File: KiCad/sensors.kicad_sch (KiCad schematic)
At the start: 26 parts, among them Q1 AO3401A, U6 LTR-303ALS-01, U8 GXHTC3

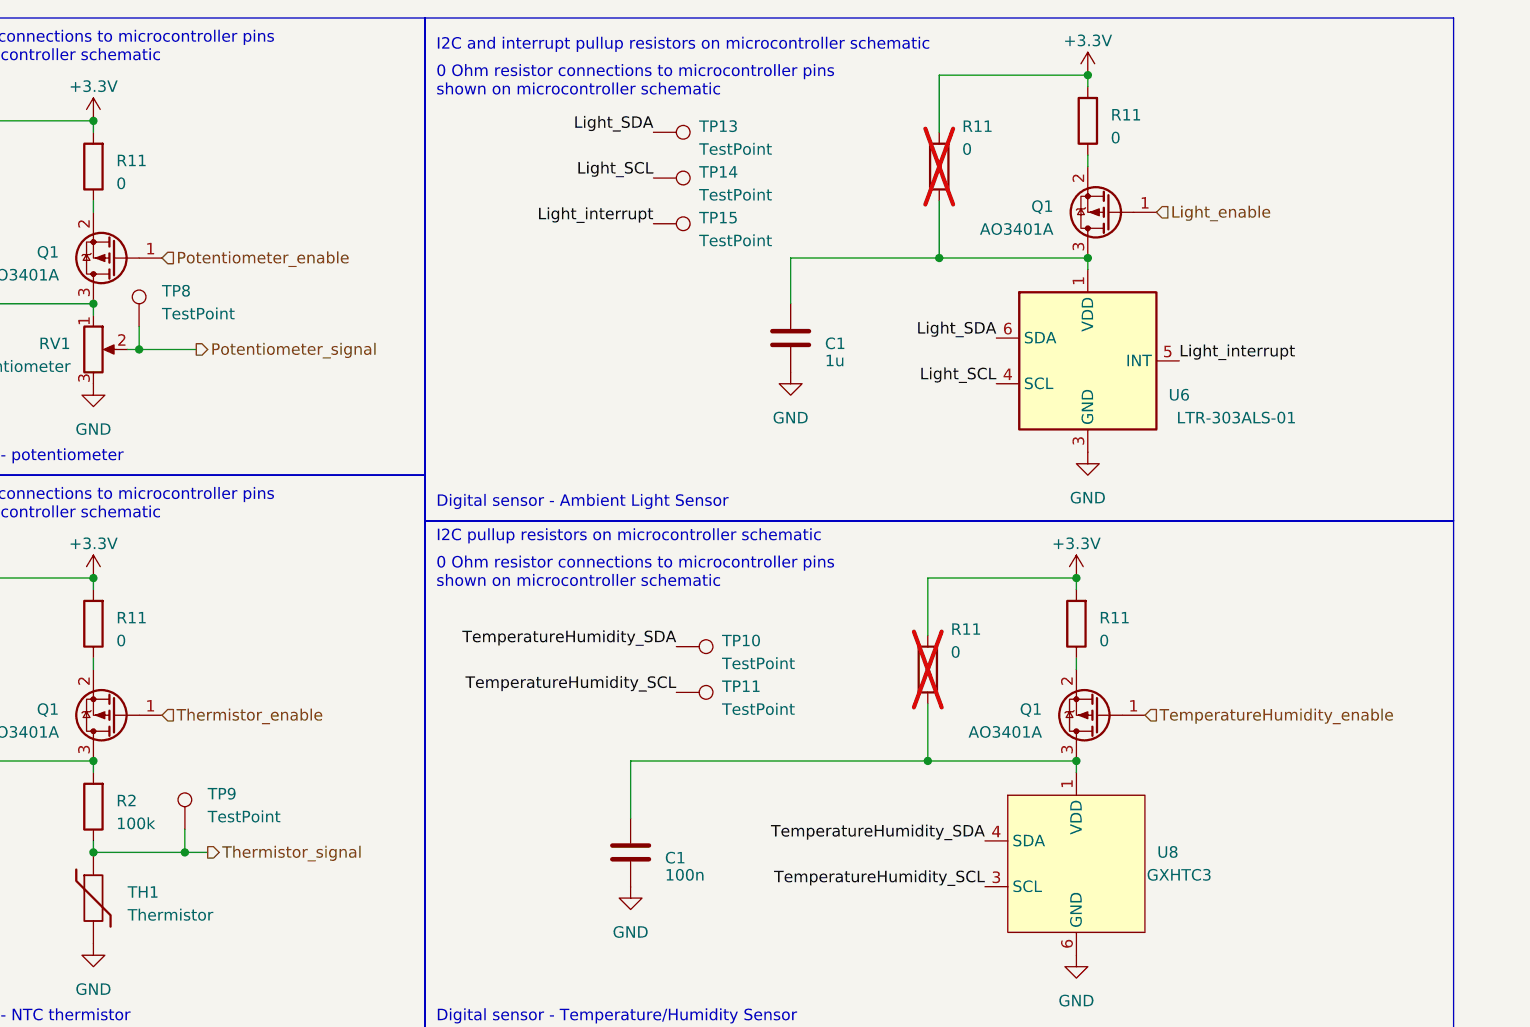
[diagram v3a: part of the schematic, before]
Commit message: updated net labelling scheme on schematic, changed some port connections on microcontroller
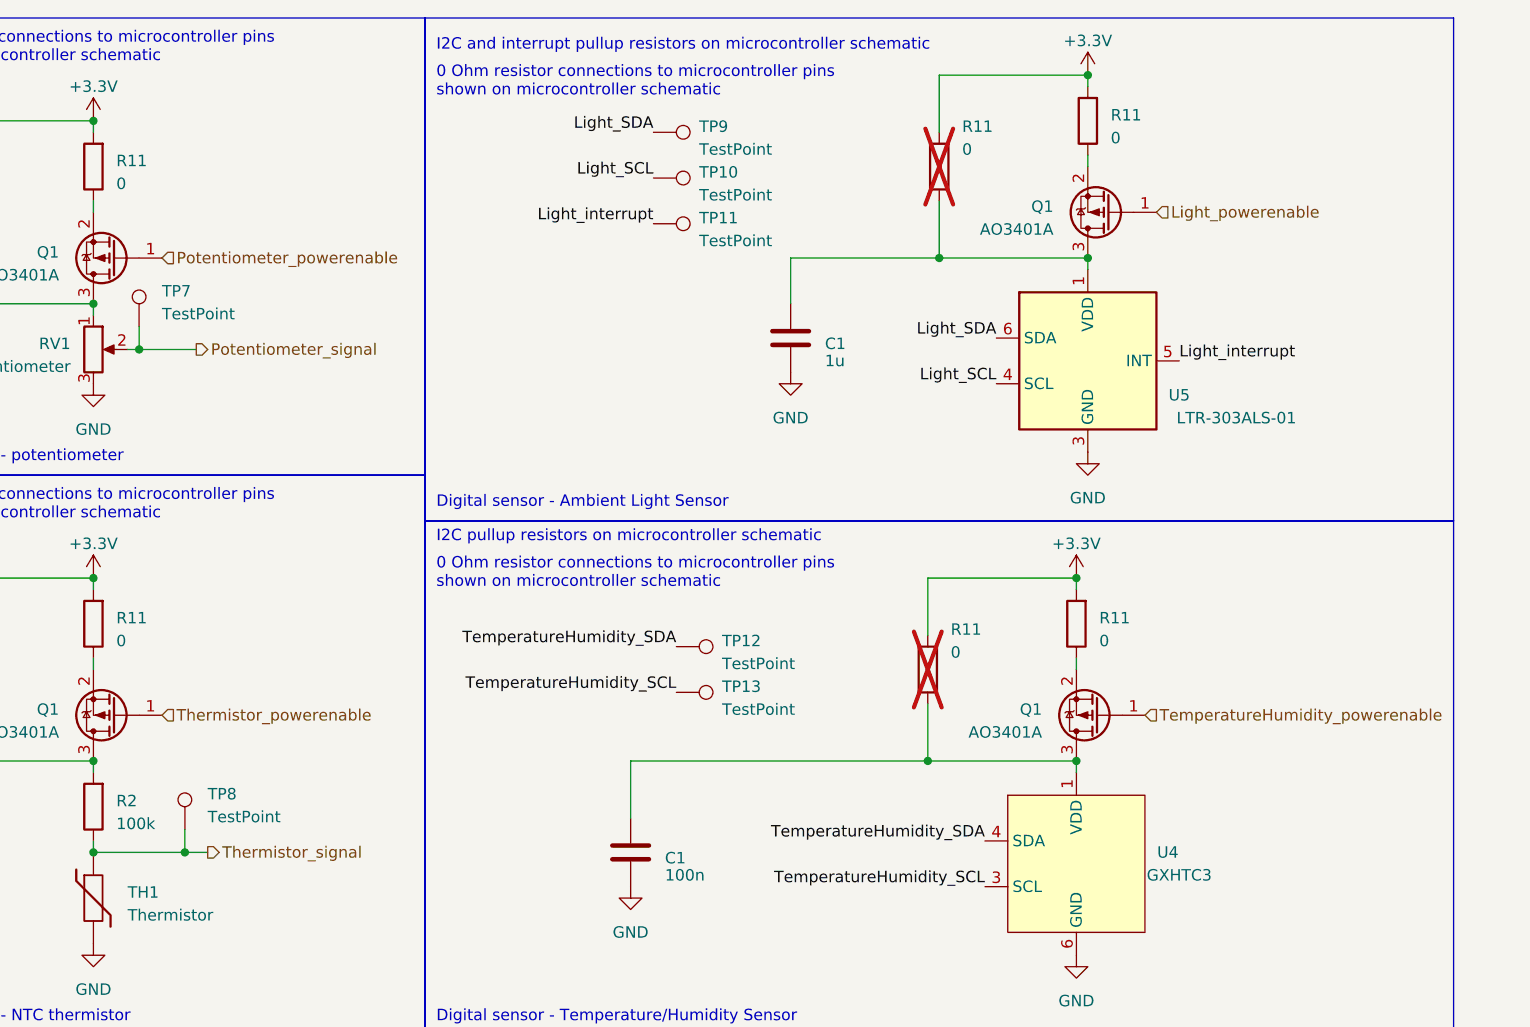
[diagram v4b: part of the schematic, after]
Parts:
- renumbered TP14 to TP10, TP15 to TP11, TP10 to TP12, TP11 to TP13, TP8 to TP7, TP9 to TP8, TP13 to TP9, U8 to U4, U6 to U5
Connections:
- net Light_enable renamed Light_powerenable
- net Potentiometer_enable renamed Potentiometer_powerenable
- net TemperatureHumidity_enable renamed TemperatureHumidity_powerenable
- net Thermistor_enable renamed Thermistor_powerenable

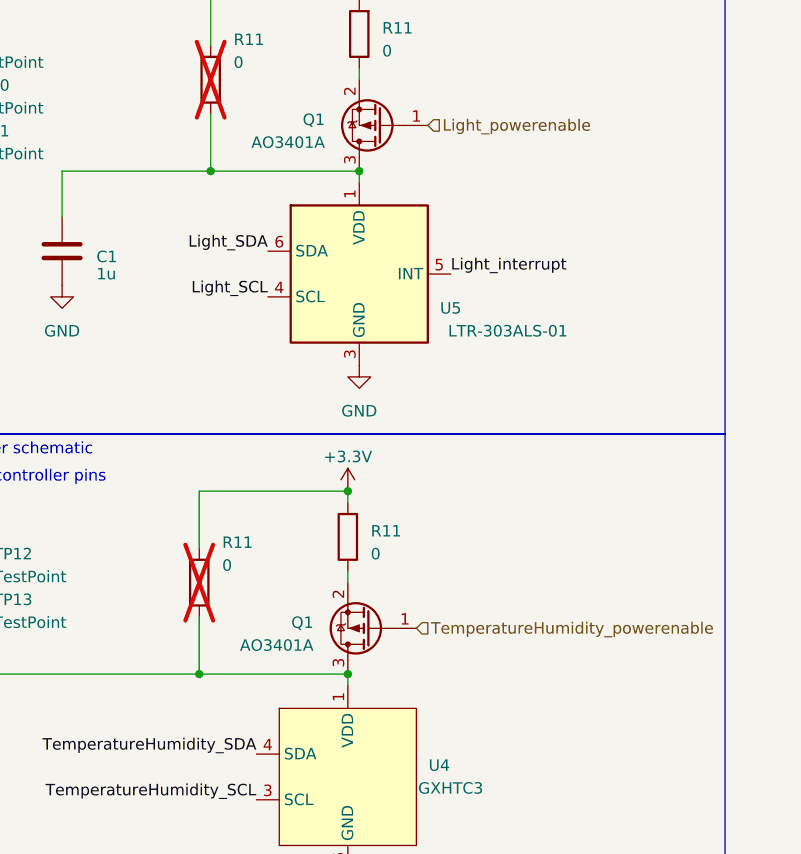
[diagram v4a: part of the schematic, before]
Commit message: ran ERCs and fixed the errors
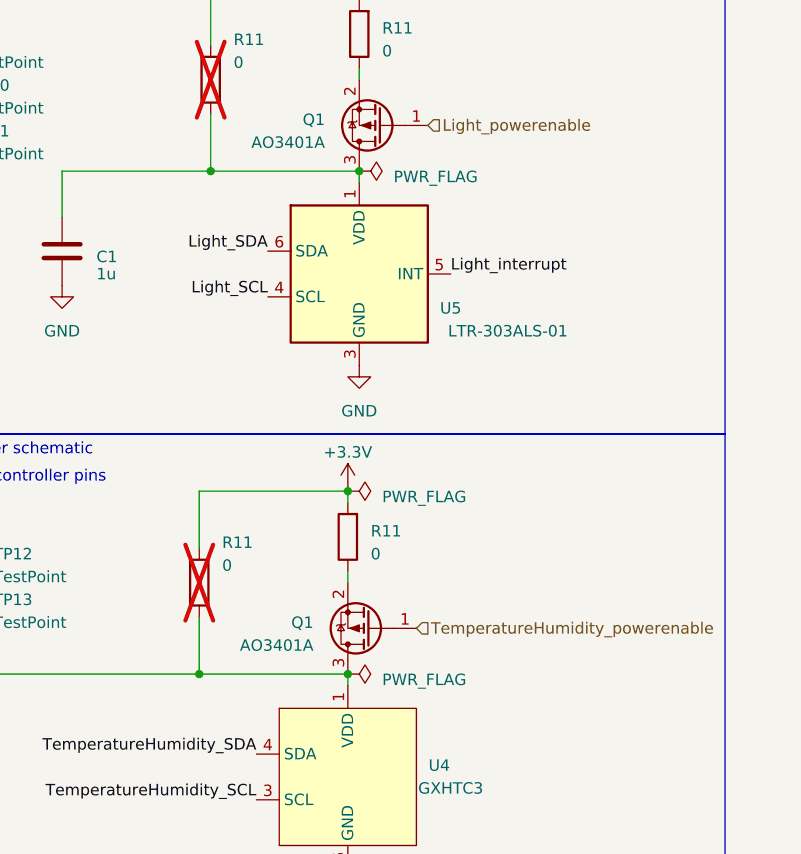
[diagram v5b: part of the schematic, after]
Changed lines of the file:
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@@
+    (stroke (width 0) (type default))
+  )
+  (wire (pts (xy 233.68 79.502) (xy 233.68 80.01))
     (stroke (width 0) (type default))
   )
@@
     )
   )
+  (symbol (lib_id "power:PWR_FLAG") (at 234.95 44.45 270) (unit 1)
+    (in_bom yes) (on_board yes) (dnp no) (fields_autoplaced)
+    (property "Reference" "#FLG06" (at 236.855 44.45 0)
+      (effects (font (size 1.27 1.27)) hide)
+    )
+    (property "Value" "PWR_FLAG" (at 238.76 45.085 90)
+      (effects (font (size 1.27 1.27)) (justify left))
+    )
+    (property "Footprint" "" (at 234.95 44.45 0)
+      (effects (font (size 1.27 1.27)) hide)
+    )
+    (property "Datasheet" "~" (at 234.95 44.45 0)
+      (effects (font (size 1.27 1.27)) hide)
+    )
+    (pin "1")
+    (instances
+      (project "EEE3088F_CKR"
+        (path "/31e5d740-f3fb-4029-be8d-dfdc4f653d72/fd4dbd89-ce5b-45e9-b49b-ec599df435f0"
+          (reference "#FLG06") (unit 1)
+        )
+      )
+    )
+  )
+  (symbol (lib_id "power:PWR_FLAG") (at 233.68 80.01 270) (unit 1)
+    (in_bom yes) (on_board yes) (dnp no) (fields_autoplaced)
+    (property "Reference" "#FLG05" (at 235.585 80.01 0)
+      (effects (font (size 1.27 1.27)) hide)
+    )
+    (property "Value" "PWR_FLAG" (at 237.49 80.645 90)
+      (effects (font (size 1.27 1.27)) (justify left))
+    )
+    (property "Footprint" "" (at 233.68 80.01 0)
+      (effects (font (size 1.27 1.27)) hide)
+    )
+    (property "Datasheet" "~" (at 233.68 80.01 0)
+      (effects (font (size 1.27 1.27)) hide)
+    )
+    (pin "1")
+    (instances
+      (project "EEE3088F_CKR"
+        (path "/31e5d740-f3fb-4029-be8d-dfdc4f653d72/fd4dbd89-ce5b-45e9-b49b-ec599df435f0"
+          (reference "#FLG05") (unit 1)
+        )
+      )
+    )
+  )
   (symbol (lib_id "power:GND") (at 184.15 114.3 0) (unit 1)
     (in_bom yes) (on_board yes) (dnp no) (fields_autoplaced)
@@
     )
   )
-  (symbol (lib_id "power:+3.3V") (at 233.68 80.01 0) (unit 1)
-    (in_bom yes) (on_board yes) (dnp no) (fields_autoplaced)
-    (property "Reference" "#PWR025" (at 233.68 83.82 0)
-      (effects (font (size 1.27 1.27)) hide)
-    )
-    (property "Value" "+3.3V" (at 233.68 76.2 0)
+  (symbol (lib_id "power:+3.3V") (at 233.68 79.502 0) (unit 1)
+    (in_bom yes) (on_board yes) (dnp no) (fields_autoplaced)
+    (property "Reference" "#PWR025" (at 233.68 83.312 0)
+      (effects (font (size 1.27 1.27)) hide)
+    )
+    (property "Value" "+3.3V" (at 233.68 75.692 0)
       (effects (font (size 1.27 1.27)))
     )
-    (property "Footprint" "" (at 233.68 80.01 0)
-      (effects (font (size 1.27 1.27)) hide)
-    )
-    (property "Datasheet" "" (at 233.68 80.01 0)
+    (property "Footprint" "" (at 233.68 79.502 0)
+      (effects (font (size 1.27 1.27)) hide)
+    )
+    (property "Datasheet" "" (at 233.68 79.502 0)
       (effects (font (size 1.27 1.27)) hide)
     )
@@
         )
       )
+    )
+  )
+  (symbol (lib_id "power:PWR_FLAG") (at 233.68 100.33 270) (unit 1)
+    (in_bom yes) (on_board yes) (dnp no) (fields_autoplaced)
+    (property "Reference" "#FLG04" (at 235.585 100.33 0)
+      (effects (font (size 1.27 1.27)) hide)
+    )
+    (property "Value" "PWR_FLAG" (at 237.49 100.965 90)
+      (effects (font (size 1.27 1.27)) (justify left))
+    )
+    (property "Footprint" "" (at 233.68 100.33 0)
+      (effects (font (size 1.27 1.27)) hide)
+    )
+    (property "Datasheet" "~" (at 233.68 100.33 0)
+      (effects (font (size 1.27 1.27)) hide)
+    )
+    (pin "1")
+    (instances
+      (project "EEE3088F_CKR"
+        (path "/31e5d740-f3fb-4029-be8d-dfdc4f653d72/fd4dbd89-ce5b-45e9-b49b-ec599df435f0"
+          (reference "#FLG04") (unit 1)
+        )
+      )

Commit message: bom updated and test labes renamed
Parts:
- C1: Extended Part Cost (none) -> 0; JLC code (none) -> C52923; Part name (none) -> CL05A105KA5NQNC; cost per unit (none) -> 0,0039
- C1: Extended Part Cost (none) -> 0; JLC code (none) -> C1525; Part name (none) -> CL05B104KO5NNNC; cost per unit (none) -> 0.0011
- R11: Extended Part Cost (none) -> 0; JLC code (none) -> C21189; Part name (none) -> 0603WAF0000T5E
- R2: Extended Part Cost (none) -> 0; cost per unit (none) -> 0,0031
- RV1: Extended Part Cost (none) -> 3; JLC code (none) -> C388854; Part name (none) -> RK09K1130AJ3; cost per unit (none) -> 0,5956
- TH1: Extended Part Cost (none) -> 3; JLC code (none) -> C77130; Part name (none) -> NCP15WF104F03RC; cost per unit (none) -> 0.0130
- TP10, TP11, TP12, TP13, TP7, TP8, TP9: Extended Part Cost (none) -> 0; cost per unit (none) -> 0
- U4: Extended Part Cost (none) -> 3; JLC code (none) -> C2837688; Part name (none) -> GXHTC3; cost per unit (none) -> 0,8714
- U5: Extended Part Cost (none) -> 3; JLC code (none) -> C364577; Part name (none) -> LTR-303ALS-01; cost per unit (none) -> 0,3762

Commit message: lots of suf for pcb diseng
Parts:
- R11: cost per unit (none) -> 0,0010
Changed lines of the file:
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@@
       (effects (font (size 1.27 1.27)) hide)
     )
-    (property "cost per unit" "" (at 234.95 29.21 0)
+    (property "cost per unit" "0,0010" (at 234.95 29.21 0)
       (effects (font (size 1.27 1.27)) hide)
     )
@@
       (effects (font (size 1.27 1.27)) hide)
     )
-    (property "cost per unit" "" (at 233.68 85.09 0)
+    (property "cost per unit" "0,0010" (at 233.68 85.09 0)
       (effects (font (size 1.27 1.27)) hide)
     )
@@
       (effects (font (size 1.27 1.27)) hide)
     )
-    (property "cost per unit" "" (at 124.46 85.09 0)
+    (property "cost per unit" "0,0010" (at 124.46 85.09 0)
       (effects (font (size 1.27 1.27)) hide)
     )
@@
       (effects (font (size 1.27 1.27)) hide)
     )
-    (property "cost per unit" "" (at 217.17 90.17 0)
+    (property "cost per unit" "0,0010" (at 217.17 90.17 0)
       (effects (font (size 1.27 1.27)) hide)
     )
@@
       (effects (font (size 1.27 1.27)) hide)
     )
-    (property "cost per unit" "" (at 218.44 34.29 0)
+    (property "cost per unit" "0,0010" (at 218.44 34.29 0)
       (effects (font (size 1.27 1.27)) hide)
     )
@@
       (effects (font (size 1.27 1.27)) hide)
     )
-    (property "cost per unit" "" (at 107.95 90.17 0)
+    (property "cost per unit" "0,0010" (at 107.95 90.17 0)
       (effects (font (size 1.27 1.27)) hide)
     )
@@
       (effects (font (size 1.27 1.27)) hide)
     )
-    (property "cost per unit" "" (at 124.46 34.29 0)
+    (property "cost per unit" "0,0010" (at 124.46 34.29 0)
       (effects (font (size 1.27 1.27)) hide)
     )
@@
       (effects (font (size 1.27 1.27)) hide)
     )
-    (property "cost per unit" "" (at 107.95 39.37 0)
-      (effects (font (size 1.27 1.27)) hide)
-    )
+    (property "cost per unit" "0,0010" (at 107.95 39.37 0)
+      (effects (font (size 1.27 1.27)) hide)
+    )
